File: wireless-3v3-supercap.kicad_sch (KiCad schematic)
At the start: 5 parts, among them J1 POWER-OUT, SW1 MODE

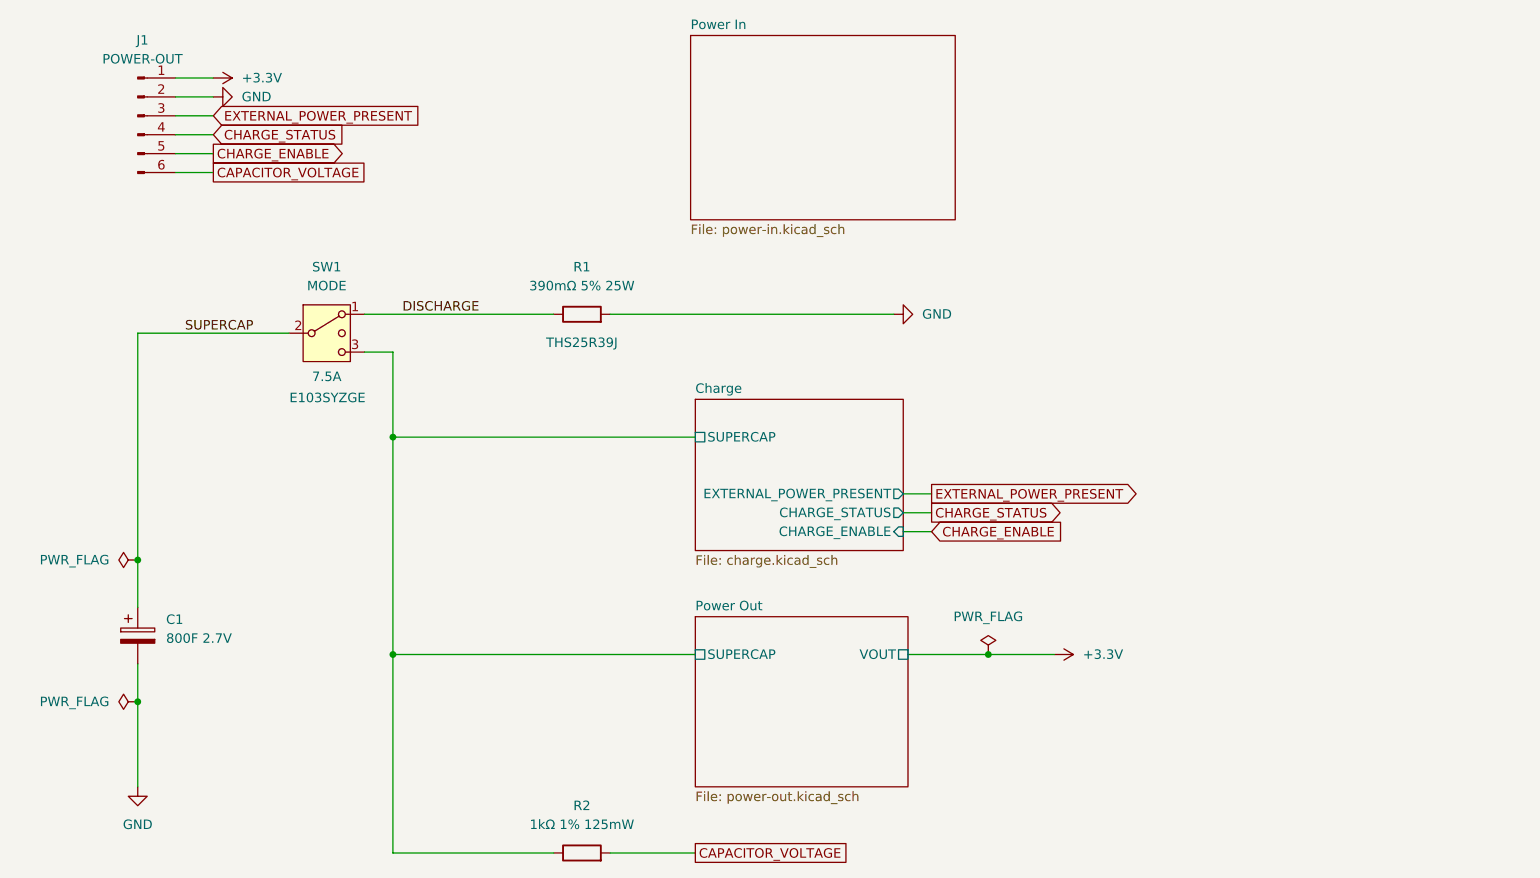
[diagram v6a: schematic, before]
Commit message: Add inductor and finish power out layout
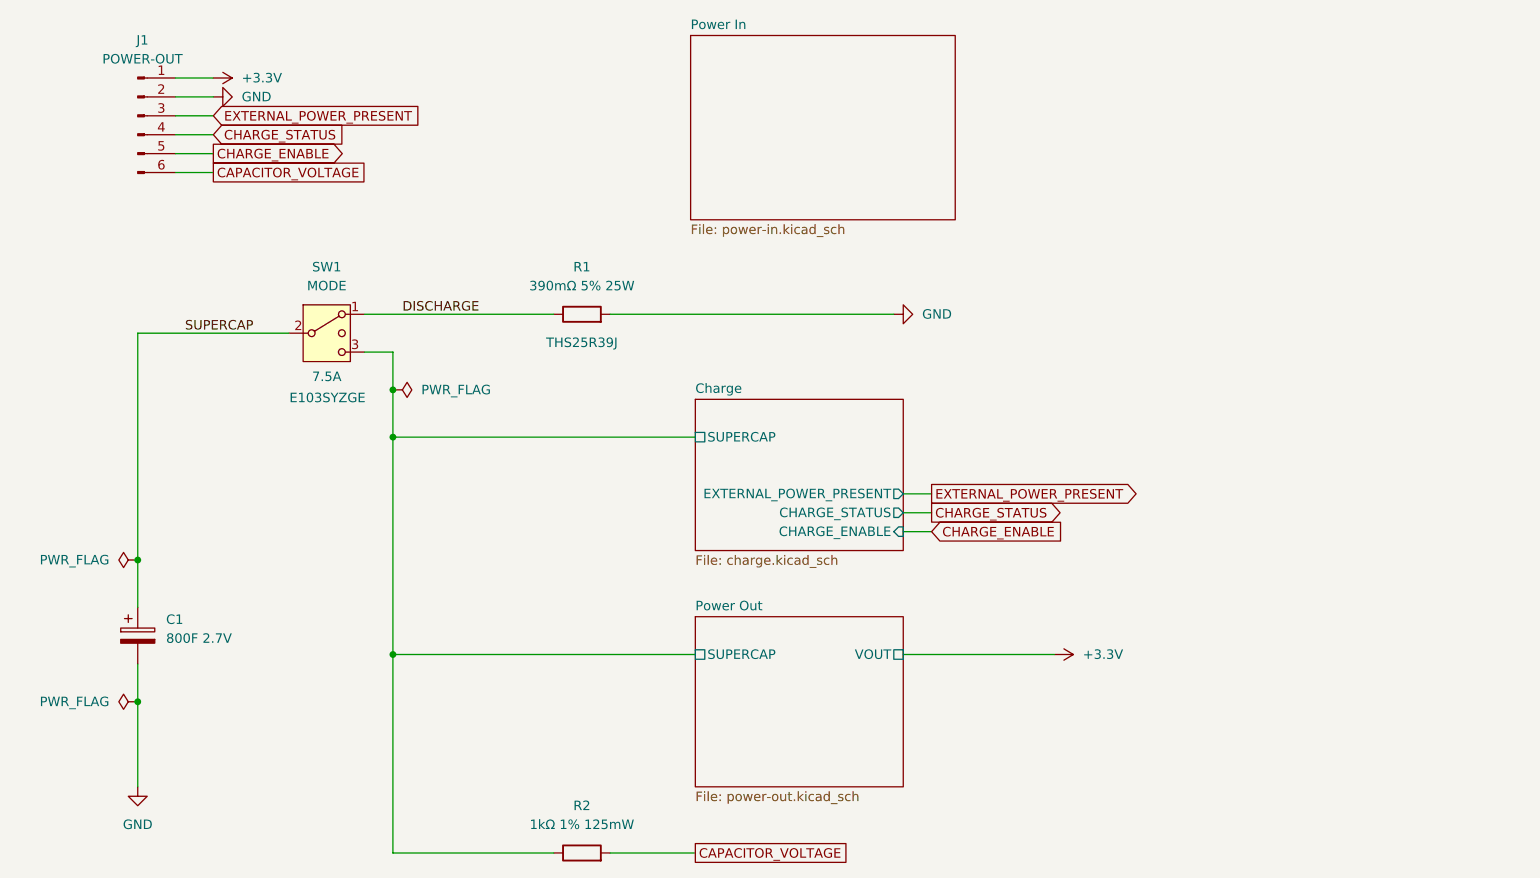
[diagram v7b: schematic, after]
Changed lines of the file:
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@@
 	)
 	(junction
-		(at 139.7 92.71)
+		(at 59.69 57.15)
 		(diameter 0)
 		(color 0 0 0 0)
@@
 	(wire
 		(pts
-			(xy 59.69 52.07) (xy 59.69 63.5)
+			(xy 59.69 52.07) (xy 59.69 57.15)
 		)
 		(stroke
@@
 	(wire
 		(pts
+			(xy 59.69 57.15) (xy 59.69 63.5)
+		)
+		(stroke
+			(width 0)
+			(type default)
+		)
+	)
+	(wire
+		(pts
 			(xy 25.4 93.98) (xy 25.4 99.06)
 		)
@@
 	(wire
 		(pts
-			(xy 128.905 92.71) (xy 139.7 92.71)
-		)
-		(stroke
-			(width 0)
-			(type default)
-		)
-	)
-	(wire
-		(pts
 			(xy 55.88 46.99) (xy 81.28 46.99)
 		)
@@
 	(wire
 		(pts
-			(xy 139.7 92.71) (xy 148.59 92.71)
-		)
-		(stroke
-			(width 0)
-			(type default)
-		)
-	)
-	(wire
-		(pts
 			(xy 59.69 92.71) (xy 59.69 119.38)
 		)
@@
 		(pts
 			(xy 30.48 15.24) (xy 35.56 15.24)
+		)
+		(stroke
+			(width 0)
+			(type default)
+		)
+	)
+	(wire
+		(pts
+			(xy 128.27 92.71) (xy 148.59 92.71)
 		)
 		(stroke
@@
 				(justify left)
 				(hide yes)
-			)
-		)
-	)
-	(symbol
-		(lib_id "power:PWR_FLAG")
-		(at 139.7 92.71 0)
-		(unit 1)
-		(exclude_from_sim no)
-		(in_bom yes)
-		(on_board yes)
-		(dnp no)
-		(fields_autoplaced yes)
-		(property "Reference" "#FLG03"
-			(at 139.7 90.805 0)
-			(effects
-				(font
-					(size 1.27 1.27)
-				)
-				(hide yes)
-			)
-		)
-		(property "Value" "PWR_FLAG"
-			(at 139.7 87.63 0)
-			(effects
-				(font
-					(size 1.27 1.27)
-				)
-			)
-		)
-		(property "Footprint" ""
-			(at 139.7 92.71 0)
-			(effects
-				(font
-					(size 1.27 1.27)
-				)
-				(hide yes)
-			)
-		)
-		(property "Datasheet" "~"
-			(at 139.7 92.71 0)
-			(effects
-				(font
-					(size 1.27 1.27)
-				)
-				(hide yes)
-			)
-		)
-		(property "Description" "Special symbol for telling ERC where power comes from"
-			(at 139.7 92.71 0)
-			(effects
-				(font
-					(size 1.27 1.27)
-				)
-				(hide yes)
-			)
-		)
-		(pin "1"
-		)
-		(instances
-			(project ""
-				(path "/01e6e533-9ed1-4dde-bac5-1959ff8991e5"
-					(reference "#FLG03")
-					(unit 1)
-				)
 			)
 		)
@@
 	)
 	(symbol
+		(lib_id "power:PWR_FLAG")
+		(at 59.69 57.15 270)
+		(unit 1)
+		(exclude_from_sim no)
+		(in_bom yes)
+		(on_board yes)
+		(dnp no)
+		(fields_autoplaced yes)
+		(property "Reference" "#FLG03"
+			(at 61.595 57.15 0)
+			(effects
+				(font
+					(size 1.27 1.27)
+				)
+				(hide yes)
+			)
+		)
+		(property "Value" "PWR_FLAG"
+			(at 63.5 57.1499 90)
+			(effects
+				(font
+					(size 1.27 1.27)
+				)
+				(justify left)
+			)
+		)
+		(property "Footprint" ""
+			(at 59.69 57.15 0)
+			(effects
+				(font
+					(size 1.27 1.27)
+				)
+				(hide yes)
+			)
+		)
+		(property "Datasheet" "~"
+			(at 59.69 57.15 0)
+			(effects
+				(font
+					(size 1.27 1.27)
+				)
+				(hide yes)
+			)
+		)
+		(property "Description" "Special symbol for telling ERC where power comes from"
+			(at 59.69 57.15 0)
+			(effects
+				(font
+					(size 1.27 1.27)
+				)
+				(hide yes)
+			)
+		)
+		(pin "1"
+		)
+		(instances
+			(project "wireless-3v3-supercap"
+				(path "/01e6e533-9ed1-4dde-bac5-1959ff8991e5"
+					(reference "#FLG03")
+					(unit 1)
+				)
+			)
+		)
+	)
+	(symbol
 		(lib_id "power:+3.3V")
 		(at 148.59 92.71 270)
@@
 	(sheet
 		(at 100.33 87.63)
-		(size 28.575 22.86)
+		(size 27.94 22.86)
 		(exclude_from_sim no)
 		(in_bom yes)
@@
 		)
 		(pin "VOUT" passive
-			(at 128.905 92.71 0)
-			(effects
-				(font
+			(at 128.27 92.71 0)
+			(effects
+				(font

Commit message: Prefix all of the references so that the numbering is manageable across multiple circuits
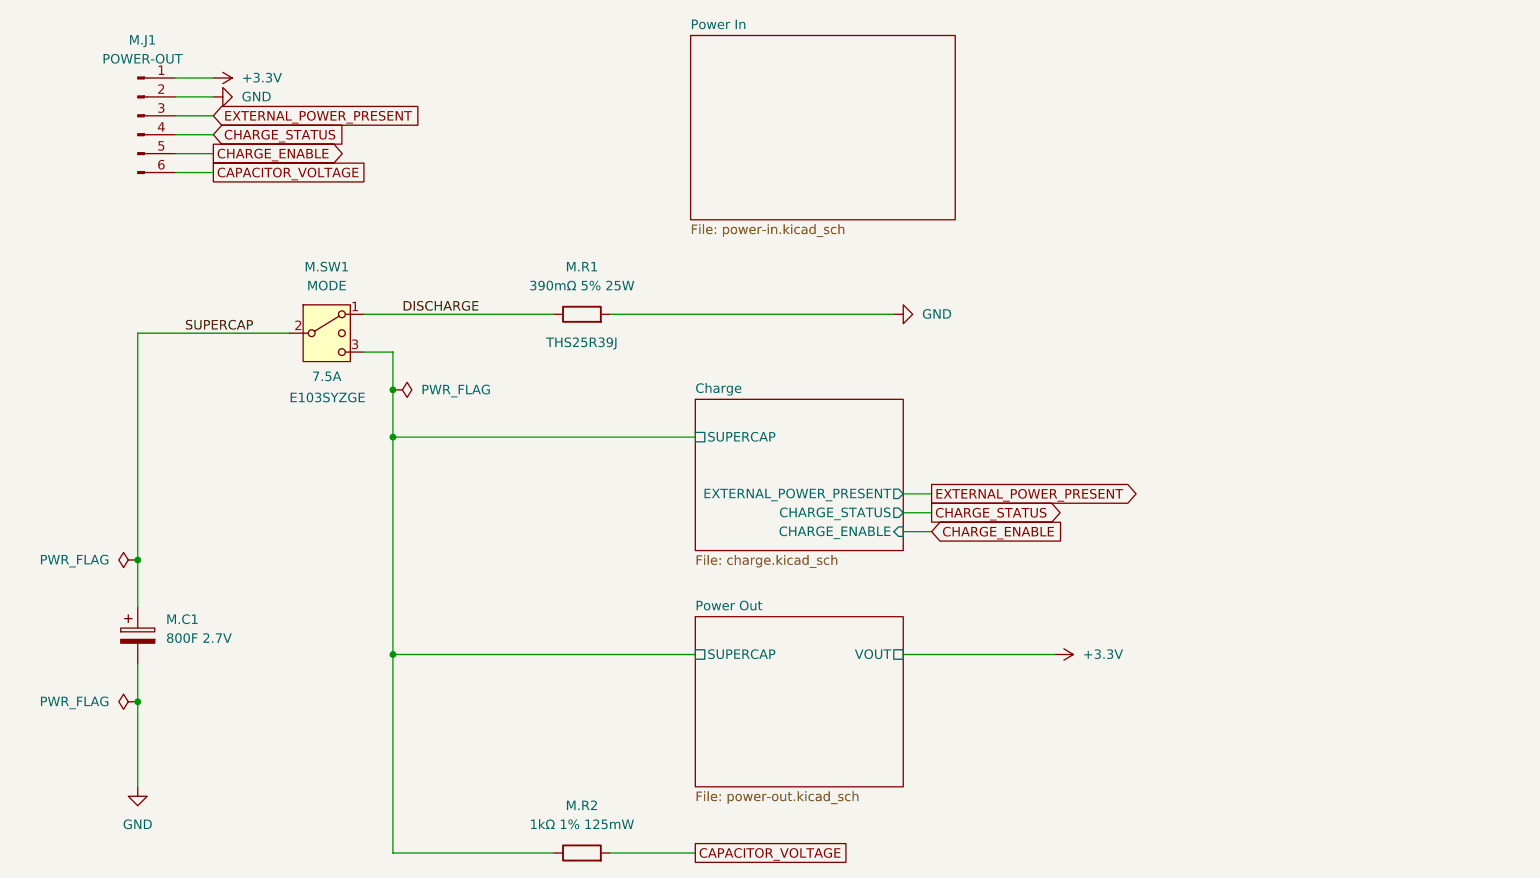
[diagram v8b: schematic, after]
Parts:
- renumbered C1 to M.C1, J1 to M.J1, R1 to M.R1, R2 to M.R2, SW1 to M.SW1
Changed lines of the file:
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@@
 		(dnp no)
 		(fields_autoplaced yes)
-		(property "Reference" "J1"
+		(property "Reference" "M.J1"
 			(at 26.035 10.16 0)
 			(effects
@@
 			(project ""
 				(path "/01e6e533-9ed1-4dde-bac5-1959ff8991e5"
-					(reference "J1")
+					(reference "M.J1")
 					(unit 1)
 				)
@@
 		(on_board yes)
 		(dnp no)
-		(property "Reference" "R1"
+		(property "Reference" "M.R1"
 			(at 85.09 40.64 90)
 			(effects
@@
 			(project ""
 				(path "/01e6e533-9ed1-4dde-bac5-1959ff8991e5"
-					(reference "R1")
+					(reference "M.R1")
 					(unit 1)
 				)
@@
 		(dnp no)
 		(fields_autoplaced yes)
-		(property "Reference" "R2"
+		(property "Reference" "M.R2"
 			(at 85.09 113.03 90)
 			(effects
@@
 			(project ""
 				(path "/01e6e533-9ed1-4dde-bac5-1959ff8991e5"
-					(reference "R2")
+					(reference "M.R2")
 					(unit 1)
 				)
@@
 		(on_board yes)
 		(dnp no)
-		(property "Reference" "SW1"
+		(property "Reference" "M.SW1"
 			(at 50.8 40.64 0)
 			(effects
@@
 			(project ""
 				(path "/01e6e533-9ed1-4dde-bac5-1959ff8991e5"
-					(reference "SW1")
+					(reference "M.SW1")
 					(unit 1)
 				)
@@
 		(dnp no)
 		(fields_autoplaced yes)
-		(property "Reference" "C1"
+		(property "Reference" "M.C1"
 			(at 29.21 88.0109 0)
 			(effects
@@
 			(project ""
 				(path "/01e6e533-9ed1-4dde-bac5-1959ff8991e5"
-					(reference "C1")
-					(unit 1)
-				)
+					(reference "M.C1")
+					(unit 1)
+				)
